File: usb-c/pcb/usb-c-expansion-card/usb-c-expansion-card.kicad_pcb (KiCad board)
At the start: 4 copper layers, 26 x 30 mm, 15 parts, among them J1 USB_C_Receptacle, P1 USB_C_Plug, U1 USBLC6-2SC6, U2 USBLC6-2SC6, U3 USBLC6-2SC6

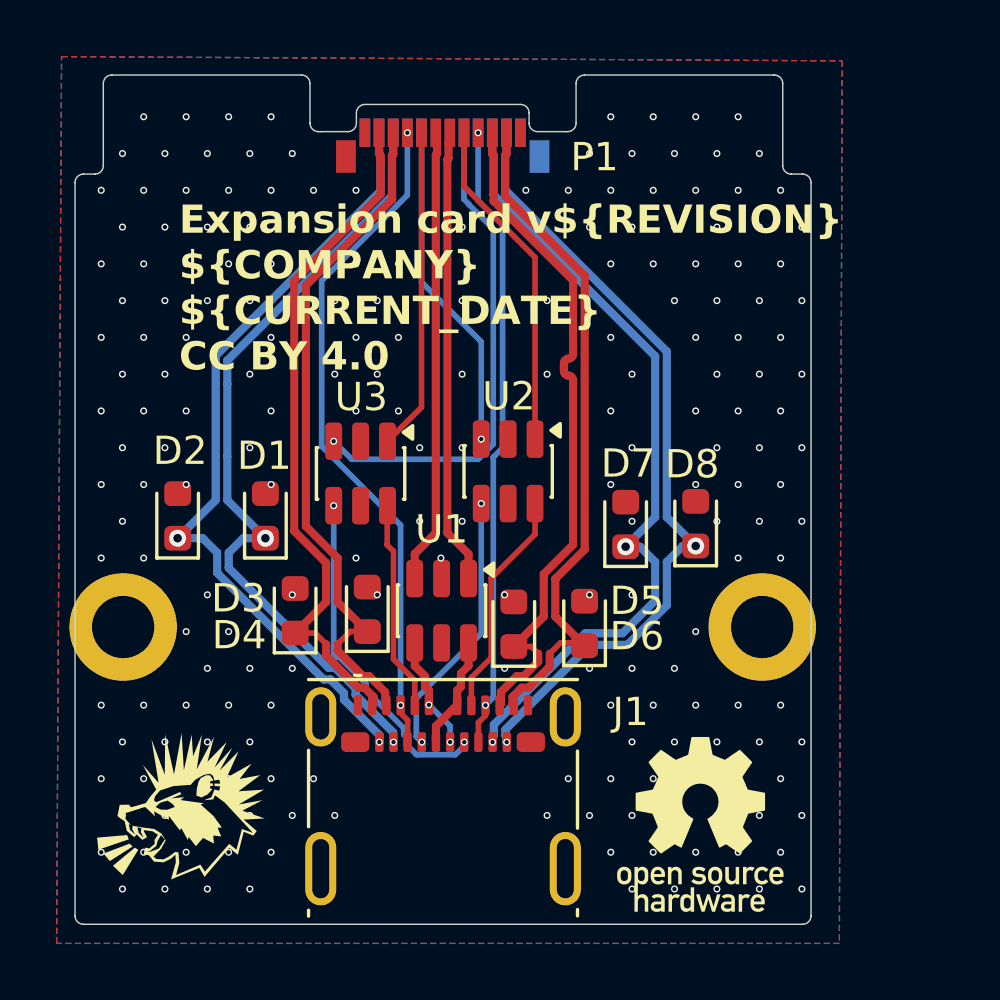
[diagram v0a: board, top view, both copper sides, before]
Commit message: prepare for partial rewire for better USB-C receptacle footprint
Signed-off-by: Lucy <user@domain.tld>
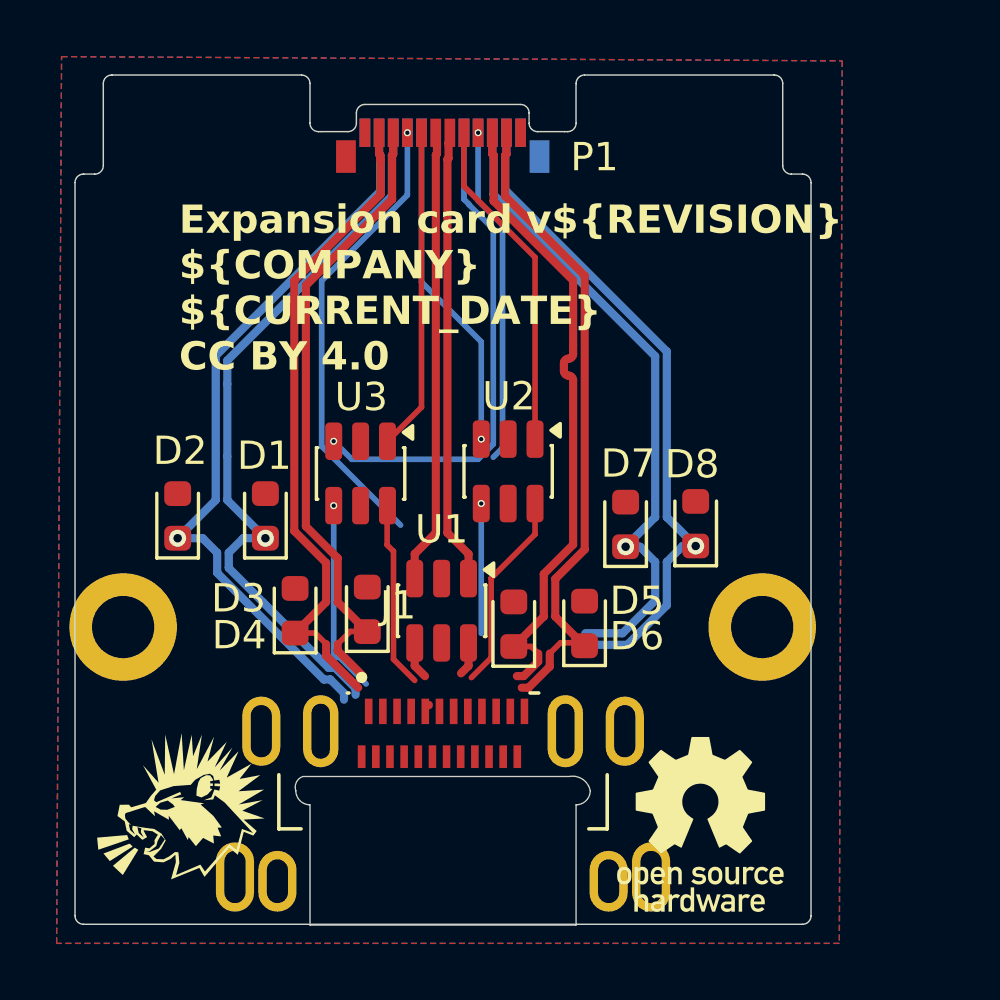
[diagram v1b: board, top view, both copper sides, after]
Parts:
- J1: footprint Connector_USB:USB_C_Receptacle_Molex_105450-0101 -> AMPHENOL-12402075E512A:AMPHENOL_12402075E512A
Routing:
- net /VBUS: track 46.3 -> 28.2 mm, vias 4 -> 2
- net /ESD_TX2_N: track 28.2 -> 23.0 mm, vias 2 -> 1
- net /CC2: track 12.1 -> 6.89 mm, vias 2 -> 1
- net /IN_SBU2: track 9.46 -> 4.59 mm, vias 2 -> 1
- net /ESD_TX2_P: track 28.2 -> 23.5 mm, vias 2 -> 1
- net /IN_D_N: track 4.35 -> 1.55 mm
- net /IN_D_P: track 4.40 -> 1.69 mm, vias 2 -> 0
- net /ESD_RX1_N: track 28.1 -> 25.8 mm, vias 2 -> 1
- net /ESD_RX1_P: track 28.1 -> 26.1 mm, vias 2 -> 1
- net /ESD_TX1_N: track 24.0 -> 22.5 mm
- net /ESD_RX2_N: track 24.0 -> 22.8 mm
- net /ESD_TX1_P: track 24.1 -> 23.1 mm
- net /IN_SBU1: track 8.06 -> 7.08 mm
- net /CC1: track 7.46 -> 6.60 mm
- net /ESD_RX2_P: track 24.1 -> 23.4 mm
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
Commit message: Board finished with new footprint
Signed-off-by: Lucy <user@domain.tld>
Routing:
- net /VBUS: track 28.2 -> 54.5 mm, vias 2 -> 4
- net /IN_SBU2: track 4.59 -> 11.4 mm, vias 1 -> 2
- net /ESD_TX2_N: track 23.0 -> 28.8 mm, vias 1 -> 2
- net /ESD_TX2_P: track 23.5 -> 28.7 mm, vias 1 -> 2
- net /CC2: track 6.89 -> 10.7 mm, vias 1 -> 2
- net /IN_D_N: track 1.55 -> 5.14 mm
- net /IN_D_P: track 1.69 -> 4.88 mm, vias 0 -> 2
- net /ESD_RX1_N: track 25.8 -> 28.5 mm, vias 1 -> 2
- net /ESD_RX1_P: track 26.1 -> 28.6 mm, vias 1 -> 2
- net /ESD_TX1_N: track 22.5 -> 24.9 mm
- net /ESD_TX1_P: track 23.1 -> 25.0 mm
- net /ESD_RX2_N: track 22.8 -> 24.4 mm
- net /IN_SBU1: track 7.08 -> 8.33 mm
- net /CC1: track 6.60 -> 7.83 mm
- net /ESD_RX2_P: track 23.4 -> 24.5 mm
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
